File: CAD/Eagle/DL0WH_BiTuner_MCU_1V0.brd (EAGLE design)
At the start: 96.5 x 73 mm, 112 parts, among them Q0321 ABS07-32.768KHZ, U0101 STM32L476RXT_64PIN_LDO, U0521 PCAL6416APW, U2401 LM53603-Q1, U9001 TPS62051, U9401 MC33996, U9501 MC33996, U9601 MC33996, U9801 MAX232_SOIC16, U9901 MAX232_SOIC16, X2411 WIRE-TO-BOARD_5MM08_1X02, X3201 MOLEX 105017-0001, X3301 SMA_SMT_AMPHENOL-901-143, X3311 SAMTEC SMA-J-P-H-RA-TH1, X9851 WIRE-TO-BOARD_5MM08_1X02, X9852 WIRE-TO-BOARD_5MM08_1X02, X9853 WIRE-TO-BOARD_5MM08_1X02, X9951 WIRE-TO-BOARD_5MM08_1X02, X9952 WIRE-TO-BOARD_5MM08_1X02, X9953 WIRE-TO-BOARD_5MM08_1X02

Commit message: HW_1V0 - CAD/Eagle - I2C port expander not needed and removed
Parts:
- removed C0521: 100nF, df4iah_rcl:C0402
- removed R0521: 100kR, df4iah_rcl:R0402
- removed U0521: PCAL6416APW, df4iah_dataconvertion:TSSOP24_SOT355-1
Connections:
- removed net PEXPA_P0_0_R: U0521.4
- removed net PEXPA_P0_1_R: U0521.5
- removed net PEXPA_P0_2_R: U0521.6
- removed net PEXPA_P0_3_R: U0521.7
- removed net PEXPA_P0_4_R: U0521.8
- removed net PEXPA_P0_5_R: U0521.9
- removed net PEXPA_P0_6_R: U0521.10
- removed net PEXPA_P0_7_R: U0521.11
- removed net PEXPA_P1_0_R: U0521.13
- removed net PEXPA_P1_1_R: U0521.14
- removed net PEXPA_P1_2_R: U0521.15
- removed net PEXPA_P1_3_R: U0521.16
- removed net PEXPA_P1_4_R: U0521.17
- removed net PEXPA_P1_5_R: U0521.18
- removed net PEXPA_P1_6_R: U0521.19
- removed net PEXPA_P1_7_R: U0521.20
- removed net PEXPA_RESET: R0521.1, U0521.3
- net +3V3: no longer C0521.1, R0521.2, U0521.2, U0521.24
- net GND: no longer C0521.2, U0521.12, U0521.21
- net MCU_I2C1_SCL: no longer U0521.22
- net MCU_I2C1_SDA: no longer U0521.23

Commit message: HW_1V0 - CAD/Eagle - I2C port added
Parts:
- added C8901, C8902: 10nF, df4iah_rcl:C0603
- added C8911: (no value), df4iah_rcl:C0603
- added C8921: 100nF, df4iah_rcl:C0603
- added D8921, D8922: CMAD6001, df4iah_diode:SOD923
- added L8901, L8902: 10uH, df4iah_rcl:L0603
- added R8901, R8902: 1kR, df4iah_rcl:R0603
- added R8903, R8904, R8923: 10kR, df4iah_rcl:R0603
- added R8911, R8912, R8922: 47R, df4iah_rcl:R0603
- added R8921: 1MR, df4iah_rcl:R0603
- added U8911: TS5A23166, df4iah_sc-switches:R-PDSO-G8
- added U8921: OPA354, df4iah_opamp:SOT-23-5
- added X0601: (no value), df4iah_connector:2X02
- L9011: device df4iah_rcl:L_8.00MM_X_8.00MM -> df4iah_rcl:L0603
- moved R9524 32.4 mm to (69.2, 11.4), turned to 270 degrees
- moved R9424 30.6 mm to (71.1, 11.4), turned to 90 degrees
- moved R0612 26.6 mm to (72.7, 27.3), flipped to the top, turned to 90 degrees
- moved R0611 25.5 mm to (71.4, 27.3), flipped to the top, turned to 90 degrees
- moved C9011 17.6 mm to (27.9, 38.1)
- moved L9011 11.7 mm to (24.1, 38.1)
- moved R9022 2.62 mm to (21.6, 38.7)
- moved U9801 2.54 mm to (82.5, 44.5)
- moved C9801 2.54 mm to (85.1, 52.1)
- moved C9802 2.54 mm to (74.9, 48.3)
- moved C9803 2.54 mm to (74.9, 45.1)
- moved C9804 2.54 mm to (80.0, 52.1)
- moved C9805 2.54 mm to (74.9, 41.9)
- moved R9801 2.54 mm to (78.7, 35.6)
- moved R9802 2.54 mm to (86.4, 35.6)
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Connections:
- removed net MCU_I2C1_SCL: R0612.1
- removed net MCU_I2C1_SDA: R0611.1
- removed net N$1: R9901.1
- removed net N$10: R9621.1
- removed net N$11: R9622.1
- removed net N$14: R9623.1
- removed net N$16: R9624.1
- removed net N$17: R9625.1
- removed net N$18: R9626.1
- removed net N$3: R9902.1
- removed net N$30: R9524.1
- removed net N$31: R9424.1
- removed net N$4: R9903.1
- removed net N$5: R9904.1
- removed net N$6: R9801.1
- removed net N$7: R9802.1
- removed net N$8: R9803.1
- removed net N$9: R9804.1
- removed net PA12PA11_N: X3201.D-
- removed net PA12PA11_P: X3201.D+
- removed net RM_BCK: X3311.1
- new net RM_REV: L8902.2, X3311.1
- new net SWR_IN_FWD: R8902.2, R8904.2, U8911.1
- new net SWR_IN_FWD_HI: C8901.1, L8901.1, R8904.1
- new net SWR_IN_REV: R8901.2, R8903.2, U8911.5
- new net SWR_IN_REV_HI: C8902.1, L8902.1, R8903.1
- new net SWR_OP_M: D8921.A, R8921.2, U8921.4
- new net SWR_OP_OUT: D8921.C, R8922.1, U8921.1
- new net SWR_SEL_FWD: R8911.2, U8911.7
- new net SWR_SEL_PWR: R8921.1, U8911.2, U8911.6
- new net SWR_SEL_REV: R8912.2, U8911.3
- net +3V3: now also C8911.1, C8921.1, R8923.1, U8911.8, U8921.5
- net GND: now also C8901.2, C8902.2, C8911.2, C8921.2, D8922.C, R8901.1, R8902.1, U8911.4, U8921.2, U8921.3, X0601.2, X0601.4
- net PA0: now also R9901.1
- net PA1: now also R9902.1
- net PA11: now also X3201.D-
- net PA12: now also X3201.D+
- net PA15: now also R9903.1
- net PA3: now also R8912.1
- net PA5: now also R9621.1
- net PA6: now also R9622.1
- net PA7: now also R9623.1
- net PB0: now also R9624.1
- net PB1: now also R9524.1
- net PB10: now also R9802.1
- net PB11: now also R9626.1
- net PB12: now also R9803.1
- net PB13: now also R9804.1
- net PB2: now also R9424.1
- net PB6: now also R0612.1, X0601.1
- net PB7: now also R9904.1
- net PB9: now also R0611.1, X0601.3
- net PC0: now also R8922.2
- net PC1: now also R9801.1
- net PC2: now also D8922.A, R8923.2
- net PC3: now also R8911.1
- net PC4: now also R9625.1
- net RM_FWD: now also L8901.2
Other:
- board text added: "BOOT0"
- board text added: "I2C"
- board text added: "SCL"
- board text added: "SDA"

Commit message: HW_1V0 - CAD/Eagle - SWR metering added, all placed
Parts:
- removed C8902: 10nF, df4iah_rcl:C0603
- removed R8904: 10kR, df4iah_rcl:R0603
- removed U8911: TS5A23166, df4iah_sc-switches:R-PDSO-G8
- added C8951: 100nF, df4iah_rcl:C0603
- added D8901, D8911: CRS08, df4iah_diode:SOD80C
- added R8913: 100kR, df4iah_rcl:R0603
- added R8951: 1MR, df4iah_rcl:R0603
- added R8952: 47R, df4iah_rcl:R0603
- added U8951: OPA354, df4iah_opamp:SOT-23-5
- C8911: value (none) -> 10nF
- R8902: value 1kR -> 15kR
- R8903: value 10kR -> 100kR
- R8911: value 47R -> 1kR
- R8912: value 47R -> 15kR
- R8921: value 1MR -> 47R
- U8921: value OPA354 -> TS5A23166; device df4iah_opamp:SOT-23-5 -> df4iah_sc-switches:R-PDSO-G8
- moved R8912 57.5 mm to (7.62, 33.0), flipped to the bottom, turned to 270 degrees
- moved R8911 53.8 mm to (5.08, 32.4), flipped to the bottom
- moved R8921 47.5 mm to (57.1, 19.1), flipped to the top
- moved R8922 47.1 mm to (61.0, 11.4), flipped to the top
- moved C8911 9.16 mm to (5.08, 34.3), turned to 0 degrees
- moved U8921 7.10 mm to (6.35, 29.2)
- moved R8901 6.98 mm to (5.08, 24.8)
- moved R8903 6.35 mm to (7.62, 26.7), flipped to the top, turned to 0 degrees
- moved C8921 5.68 mm to (10.2, 26.7), turned to 270 degrees
- moved R8902 2.84 mm to (7.62, 24.1), turned to 90 degrees
- renumbered D8921 to D8951, D8922 to D8961, L8902 to L8911, R8923 to R8961
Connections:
- removed net SWR_OP_M: D8951.A, R8921.2, U8921.4
- net +3V3: now also C8951.1, D8901.C, D8911.C, R8903.2, R8913.2, U8921.8, U8951.5; no longer C8911.1, U8911.8, U8921.5
- net GND: now also C8951.2, R8911.1, R8951.1, U8921.4, U8951.2, U8951.3; no longer C8902.2, R8902.1, U8911.4, U8921.2, U8921.3
- net PA3: now also R8922.1; no longer R8912.1
- net PC0: now also R8952.2; no longer R8922.2
- net PC3: now also R8921.1; no longer R8911.1
- net SWR_IN_FWD: now also D8901.A, R8903.1, U8921.1; no longer R8904.2, U8911.1
- net SWR_IN_FWD_HI: now also R8901.2, R8902.1; no longer R8904.1
- net SWR_IN_REV: now also D8911.A, R8912.2, R8913.1, U8921.5; no longer R8901.2, R8903.2, U8911.5
- net SWR_IN_REV_HI: now also C8911.1, R8911.2, R8912.1; no longer C8902.1, R8903.1
- net SWR_OP_OUT: now also R8952.1, U8951.1; no longer R8922.1, U8921.1
- net SWR_SEL_FWD: now also R8921.2, U8921.7; no longer R8911.2, U8911.7
- net SWR_SEL_PWR: now also D8951.A, R8951.2, U8921.2, U8921.6, U8951.4; no longer R8921.1, U8911.2, U8911.6
- net SWR_SEL_REV: now also R8922.2, U8921.3; no longer R8912.2, U8911.3

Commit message: HW_1V0 - CAD/Eagle - some routing done
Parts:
- L9011: device df4iah_rcl:L0603 -> df4iah_rcl:L_8.00MM_X_8.00MM
- moved R9903 41.5 mm to (71.1, 25.7), flipped to the bottom
- moved R9621 33.4 mm to (66.4, 11.1), turned to 270 degrees
- moved R9901 27.8 mm to (59.1, 10.2), turned to 180 degrees
- moved R9622 25.0 mm to (67.3, 11.1), flipped to the bottom, turned to 270 degrees
- moved R9623 24.7 mm to (67.9, 11.1)
- moved R9625 24.5 mm to (68.9, 11.1), flipped to the bottom, turned to 270 degrees
- moved R9624 24.5 mm to (69.5, 11.1), turned to 270 degrees
- moved R9801 24.3 mm to (61.0, 19.1), flipped to the bottom, turned to 0 degrees
- moved R9626 22.5 mm to (76.8, 13.3), turned to 0 degrees
- moved R9803 21.1 mm to (76.8, 14.9), turned to 0 degrees
- moved R9902 12.1 mm to (38.7, 7.94), turned to 90 degrees
- moved R9802 8.16 mm to (88.3, 43.5), turned to 180 degrees
- moved R9804 6.07 mm to (88.3, 39.7), turned to 180 degrees
- moved R9021 5.71 mm to (25.4, 38.7), turned to 180 degrees
- moved R9022 4.26 mm to (25.4, 40.6), turned to 180 degrees
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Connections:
- removed net +5V0: C2421.1, C2422.1, C2423.1, C9001.1, L2411.1, R2411.2, R9002.2, U2401.9, U9001.1, U9001.8
- removed net DC_12V_IN: C2401.1, C2402.1, C2403.1, C2404.1, U2401.11, U2401.12, U2401.13, X2411.1
- net +12V: now also C2401.1, C2402.1, C2403.1, C2404.1, U2401.11, U2401.12, U2401.13, X2411.1
- net +5V: now also C2421.1, C2422.1, C2423.1, C9001.1, L2411.1, R2411.2, R9002.2, U2401.9, U9001.1, U9001.8
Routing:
- net GND: track 0.00 -> 813.4 mm, vias 0 -> 29
- net +5V: track 0.00 -> 203.3 mm, vias 0 -> 3
- net +3V3: track 0.00 -> 149.6 mm, vias 0 -> 7
- net +12V: track 0.00 -> 135.1 mm, vias 0 -> 4
- net SPI_DRV_PWM: track 0.00 -> 96.1 mm, vias 0 -> 8
- net SPI_DRV_!RST: track 0.00 -> 78.6 mm, vias 0 -> 5
- net SPI_DRV_SO: track 0.00 -> 58.6 mm, vias 0 -> 5
- net PB10: track 0.00 -> 57.7 mm, vias 0 -> 2
- net SPI_DRV_SCLK: track 0.00 -> 55.9 mm, vias 0 -> 3
- net SPI_DRV_L_!CS: track 0.00 -> 52.7 mm, vias 0 -> 3
- net MP_RS_RXD_R: track 0.00 -> 51.0 mm, vias 0 -> 3
- net PB13: track 0.00 -> 49.8 mm, vias 0 -> 2
- net PB7: track 0.00 -> 46.8 mm, vias 0 -> 2
- net MP_CAT_CTS_R: track 0.00 -> 46.6 mm, vias 0 -> 1
- net MCU_NRST: track 0.00 -> 46.0 mm, vias 0 -> 2
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
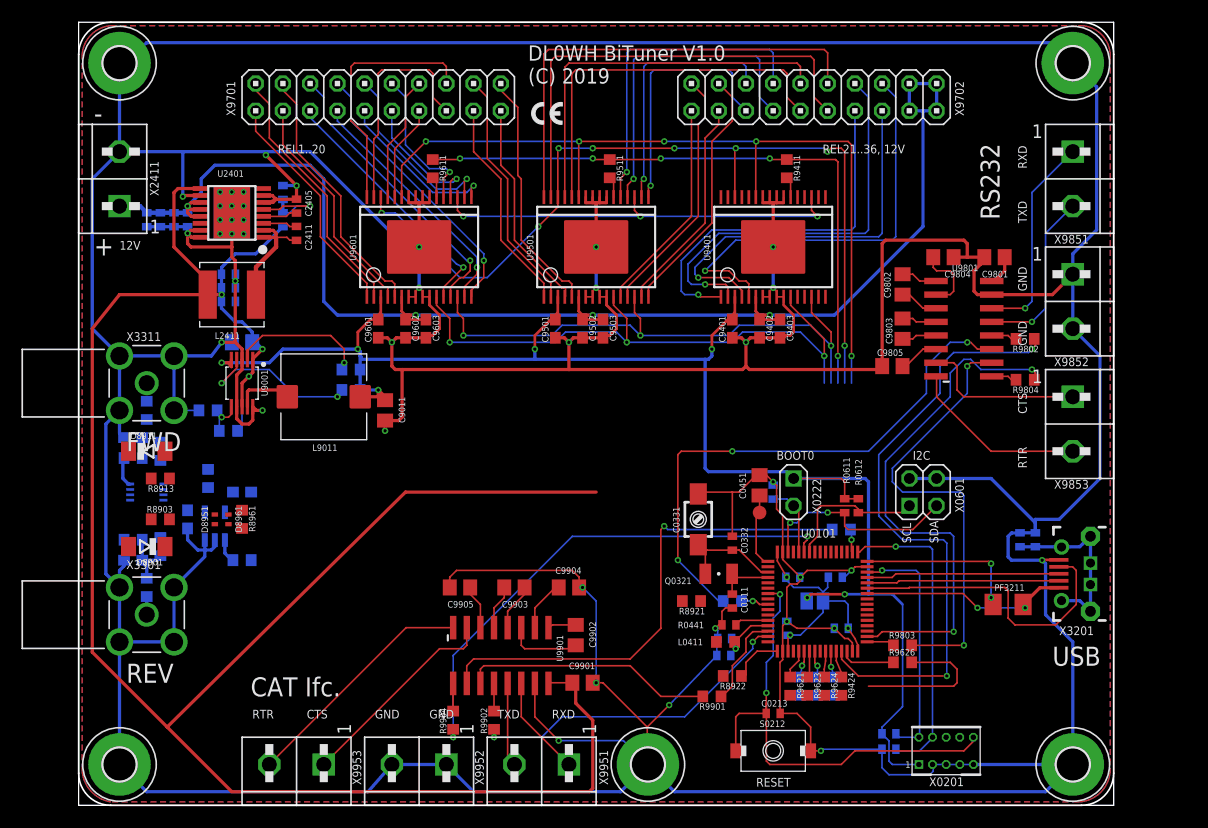
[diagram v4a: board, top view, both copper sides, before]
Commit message: HW_1V0 - CAD/Eagle - prepared BOM and adjusted some package sizes - still L9011 needs correct package
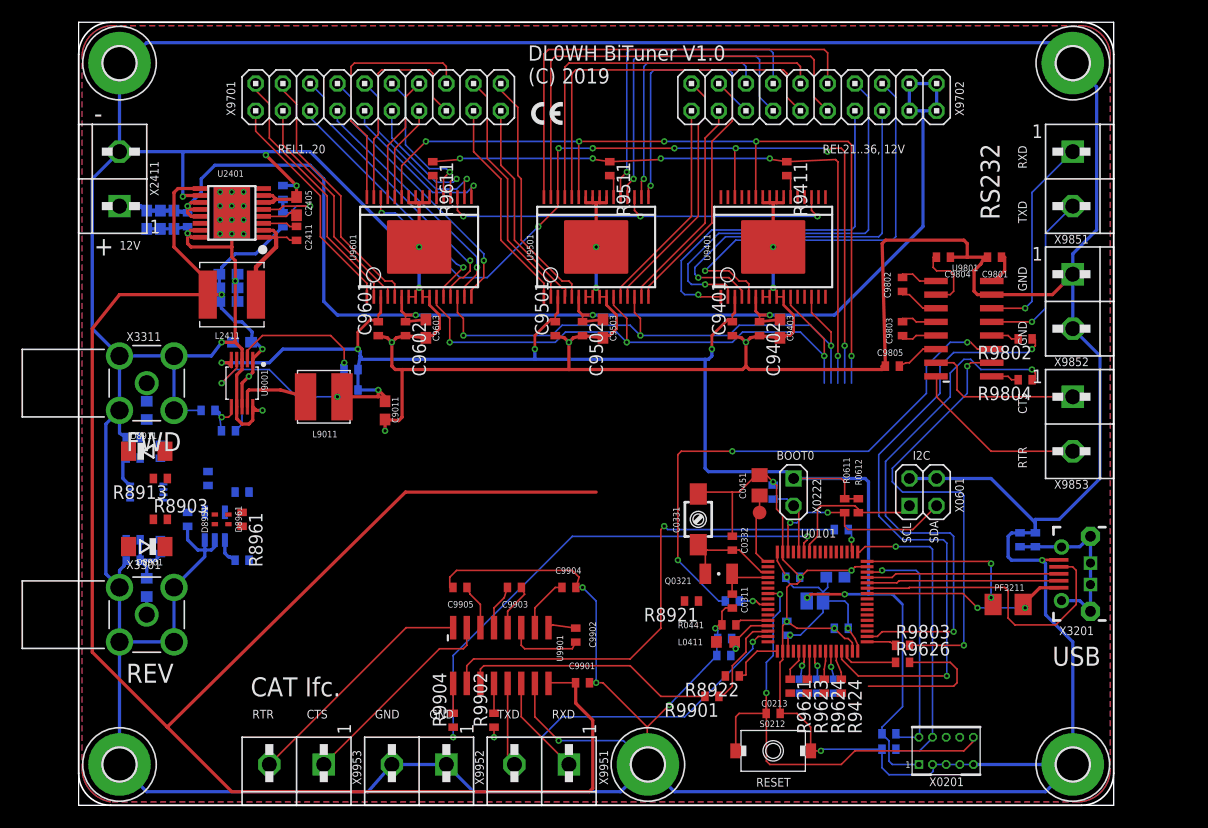
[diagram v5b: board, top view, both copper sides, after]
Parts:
- C0410, C2401, C2402, C2403, C2405, C2421, C2422, C2423: device df4iah_rcl:C0402 -> df4iah_rcl:C0603
- C8901, C8911, C8921, C8951, C9401, C9402, C9501, C9502, C9601, C9602: device df4iah_rcl:C0603 -> df4iah_rcl:C0402
- C9001, C9011: device df4iah_rcl:C0805 -> df4iah_rcl:C0603
- C9801, C9802, C9803, C9804, C9805, C9901, C9902, C9903, C9904, C9905: device rcl:C0805 -> df4iah_rcl:C0402
- L9011: device df4iah_rcl:L_8.00MM_X_8.00MM -> df4iah_rcl:L_4.90MM_X_4.90MM
- R0611, R0612: value 1.0kR -> 1kR
- R8901, R8902, R8903, R8911, R8912, R8913, R8921, R8922, R8951, R8952, R8961, R9001, R9002, R9021, R9022, R9411, R9424, R9511, R9524, R9611, R9621, R9622, R9623, R9624, R9625, R9626, R9801, R9802, R9803, R9804, R9901, R9902, R9903, R9904: device df4iah_rcl:R0603 -> df4iah_rcl:R0402
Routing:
- net GND: track 813.4 -> 816.6 mm
- net +3V3: track 149.6 -> 152.3 mm
- net TPS_SW: track 5.47 -> 6.99 mm
- net +5V: track 203.3 -> 204.2 mm
- net +12V: track 135.1 -> 135.8 mm

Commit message: HW_1V0 - CAD/Eagle - pages renumbered: 17 pages
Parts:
- removed R9611: 47R, df4iah_rcl:R0402
- added R0511: 1kR, df4iah_rcl:R0402
- R0611: value 1kR -> 47R
- moved R0611 49.6 mm to (33.0, 59.4), turned to 270 degrees
- renumbered C2401 to C1201, C2402 to C1202, C2403 to C1203, C2404 to C1204, C2405 to C1205, C2411 to C1211, C2412 to C1212, C2421 to C1221, C2422 to C1222, C2423 to C1223, C3203 to C1403, C8901 to C0901, C8911 to C0911, C8921 to C0921, C8951 to C0951, C9001 to C1301, C9011 to C1311, C9401 to C0801, C9402 to C0802, C9403 to C0803, C9501 to C0701, C9502 to C0702, C9503 to C0703, C9601 to C0601, C9602 to C0602, C9603 to C0603, C9801 to C1001, C9802 to C1002, C9803 to C1003, C9804 to C1004, C9805 to C1005, C9901 to C1101, C9902 to C1102, C9903 to C1103, C9904 to C1104, C9905 to C1105, D8901 to D0901, D8911 to D0911, D8951 to D0951, D8961 to D0961, H3611 to H1711, H3621 to H1721, H3631 to H1731, H3651 to H1751, H3661 to H1761, L2411 to L1211, L8901 to L0901, L8911 to L0911, L9011 to L1311, PF3211 to PF1411, R0612 to R0512, R2411 to R1211, R3202 to R1402, R8901 to R0901, R8902 to R0902, R8903 to R0903, R8911 to R0911, R8912 to R0912, R8913 to R0913, R8921 to R0921, R8922 to R0922, R8951 to R0951, R8952 to R0952, R8961 to R0961, R9001 to R1301, R9002 to R1302, R9021 to R1321, R9022 to R1322, R9411 to R0811, R9424 to R0824, R9511 to R0711, R9524 to R0724, R9621 to R0621, R9622 to R0622, R9623 to R0623, R9624 to R0624, R9625 to R0625, R9626 to R0626, R9801 to R1001, R9802 to R1002, R9803 to R1003, R9804 to R1004, R9901 to R1101, R9902 to R1102, R9903 to R1103, R9904 to R1104, U2401 to U1201, U8921 to U0921, U8951 to U0951, U9001 to U1301, U9401 to U0801, U9501 to U0701, U9601 to U0601, U9801 to U1001, U9901 to U1101, X2411 to X1211, X3201 to X1401, X3301 to X1501, X3311 to X1511, X9701 to X1601, X9702 to X1602, X9851 to X1051, X9852 to X1052, X9853 to X1053, X9951 to X1151, X9952 to X1152, X9953 to X1153
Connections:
- net +3V3: now also R0511.2; no longer R0611.2
- net N$12: now also R0611.2; no longer R9611.2
- net PB9: now also R0511.1; no longer R0611.1
- net SPI_DRV_SO: now also R0611.1; no longer R9611.1

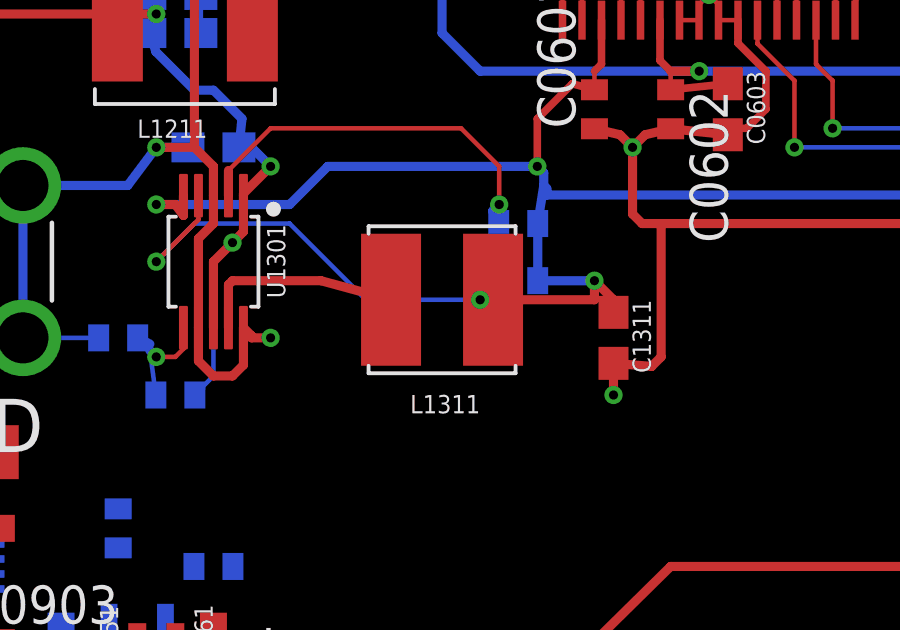
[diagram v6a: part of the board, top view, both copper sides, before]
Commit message: HW_1V0 - 10uH Murata inductivity added
Signed-off-by: Ulrich Habel <espero7757@gmx.net>
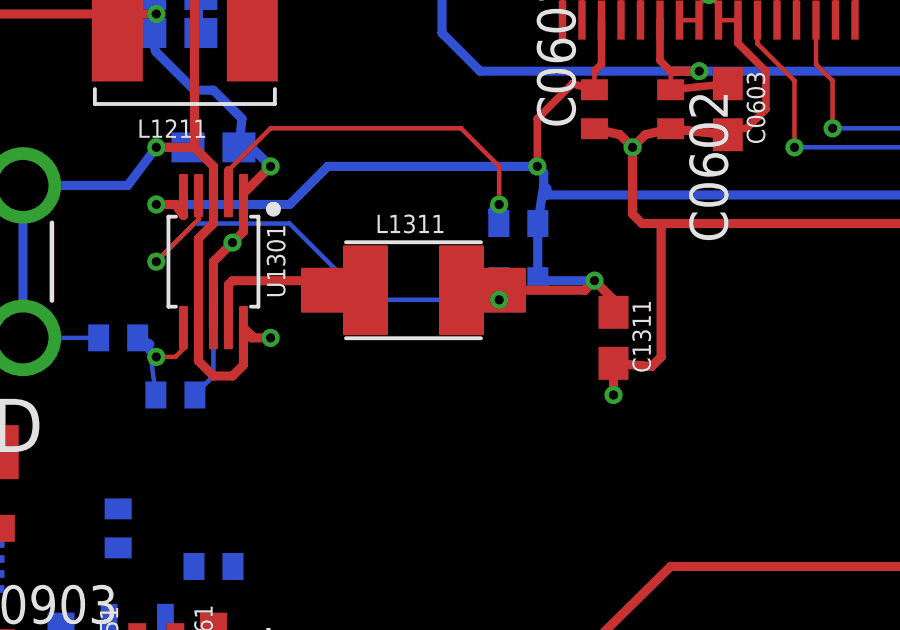
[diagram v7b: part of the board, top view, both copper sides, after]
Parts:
- L1311: device df4iah_rcl:L_4.90MM_X_4.90MM -> df4iah_rcl:L_4.50MM_X_3.20MM
- moved L1311 1.00 mm to (21.9, 38.4)
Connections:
- net +3V3: now also L1311.3
- net TPS_SW: now also L1311.4
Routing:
- net TPS_SW: track 6.99 -> 6.09 mm
- net +3V3: track 152.3 -> 152.9 mm
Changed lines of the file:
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@@
 <element name="R0824" library="df4iah_rcl" package="R0402" value="47R" x="71.12" y="11.1125" rot="R270"/>
 <element name="U1301" library="df4iah_powersupply" package="S-PDSO-G10" value="TPS62051" x="15.24" y="39.37" rot="R180"/>
-<element name="L1311" library="df4iah_rcl" package="L_4.90MM_X_4.90MM" value="10uH" x="22.86" y="38.1" rot="R180"/>
+<element name="L1311" library="df4iah_rcl" package="L_4.50MM_X_3.20MM" value="10uH" x="21.9075" y="38.4175" smashed="yes" rot="R180">
+<attribute name="NAME" x="20.6375" y="40.3225" size="0.6096" layer="25" font="vector" ratio="10"/>
+<attribute name="VALUE" x="23.1775" y="40.9575" size="0.6096" layer="27" font="vector" ratio="10" rot="R180"/>
+</element>
 <element name="R1321" library="df4iah_rcl" package="R0402" value="1MR" x="25.4" y="38.735" rot="MR180"/>
 <element name="R1322" library="df4iah_rcl" package="R0402" value="1MR" x="25.4" y="40.64" rot="MR180"/>
@@
 <wire x1="28.575" y1="37.68" x2="28.575" y2="38.1" width="0.3048" layer="1"/>
 <wire x1="28.575" y1="38.1" x2="27.94" y2="38.735" width="0.3048" layer="1"/>
-<wire x1="24.56" y1="38.1" x2="27.94" y2="38.1" width="0.3048" layer="1"/>
-<wire x1="27.94" y1="38.1" x2="27.94" y2="38.735" width="0.3048" layer="1"/>
+<wire x1="23.5075" y1="38.4175" x2="27.6225" y2="38.4175" width="0.3048" layer="1"/>
+<wire x1="27.6225" y1="38.4175" x2="27.94" y2="38.735" width="0.3048" layer="1"/>
 <wire x1="26.05" y1="38.735" x2="27.94" y2="38.735" width="0.3048" layer="16"/>
 <wire x1="26.05" y1="40.64" x2="26.05" y2="38.735" width="0.3048" layer="16"/>
@@
 <wire x1="8.05" y1="24.13" x2="8.27" y2="26.67" width="0" layer="19" extent="1-1"/>
 <wire x1="4.65" y1="33.02" x2="6.97" y2="30.48" width="0" layer="19" extent="1-1"/>
+<contactref element="L1311" pad="3"/>
 </signal>
 <signal name="P$8">
@@
 <wire x1="15.74" y1="38.6" x2="15.875" y2="38.735" width="0.3048" layer="1"/>
 <wire x1="15.875" y1="38.735" x2="18.825" y2="38.735" width="0.3048" layer="1"/>
-<wire x1="18.825" y1="38.735" x2="21.16" y2="38.1" width="0.3048" layer="1"/>
+<wire x1="18.825" y1="38.735" x2="20.3075" y2="38.4175" width="0.3048" layer="1"/>
+<contactref element="L1311" pad="4"/>
 </signal>
 <signal name="TPS_PG">
@@
 <wire x1="14.74" y1="41.57" x2="14.74" y2="40.775" width="0.1524" layer="1"/>
 <wire x1="14.74" y1="40.775" x2="13.335" y2="39.37" width="0.1524" layer="1"/>
-<via x="24.13" y="38.1" extent="1-16" drill="0.3048"/>
+<via x="24.765" y="38.1" extent="1-16" drill="0.3048"/>
 <wire x1="24.75" y1="38.735" x2="24.55" y2="38.315" width="0.1524" layer="16"/>
-<wire x1="24.55" y1="38.315" x2="24.13" y2="38.1" width="0.1524" layer="16"/>
+<wire x1="24.55" y1="38.315" x2="24.765" y2="38.1" width="0.1524" layer="16"/>
 <via x="13.335" y="39.37" extent="1-16" drill="0.3048"/>
 <wire x1="13.335" y1="39.37" x2="14.605" y2="40.64" width="0.1524" layer="16"/>
 <wire x1="14.605" y1="40.64" x2="17.78" y2="40.64" width="0.1524" layer="16"/>
 <wire x1="17.78" y1="40.64" x2="20.32" y2="38.1" width="0.1524" layer="16"/>
-<wire x1="20.32" y1="38.1" x2="24.13" y2="38.1" width="0.1524" layer="16"/>
+<wire x1="20.32" y1="38.1" x2="24.765" y2="38.1" width="0.1524" layer="16"/>
 </signal>
 <signal name="TPS_LBO">
